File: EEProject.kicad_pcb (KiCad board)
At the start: 2 copper layers, 155.4 x 20 mm, 0 parts

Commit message: Seperated Schematics
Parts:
- added P1: USB_C_Plug_USB2.0, Connector_USB:USB_C_Plug_Molex_105444, F.Cu at (104.8, 93.5)
- added U1: ATmega328-A, Package_QFP:TQFP-32_7x7mm_P0.8mm, F.Cu at (218.8, 98.3)
- added U2: 74AHC595, Package_SO:TSSOP-16_4.4x5mm_P0.65mm, F.Cu at (145.9, 94.1)
- added U3: 74AHC595, Package_SO:TSSOP-16_4.4x5mm_P0.65mm, F.Cu at (154.5, 94.0)
- added U4: 74AHC595, Package_SO:TSSOP-16_4.4x5mm_P0.65mm, F.Cu at (163.6, 94.1)
- added U5: 74AHC595, Package_SO:TSSOP-16_4.4x5mm_P0.65mm, F.Cu at (173.0, 94.0)
- added U6: CP2102N-Axx-xQFN28, Package_DFN_QFN:QFN-28-1EP_5x5mm_P0.5mm_EP3.35x3.35mm, F.Cu at (119.5, 93.5)

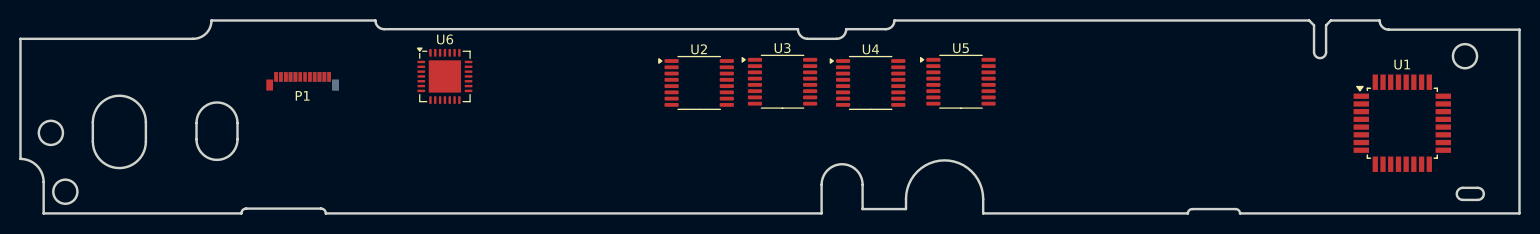
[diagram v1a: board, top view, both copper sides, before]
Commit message: Keyboard Data Changes and added footprints
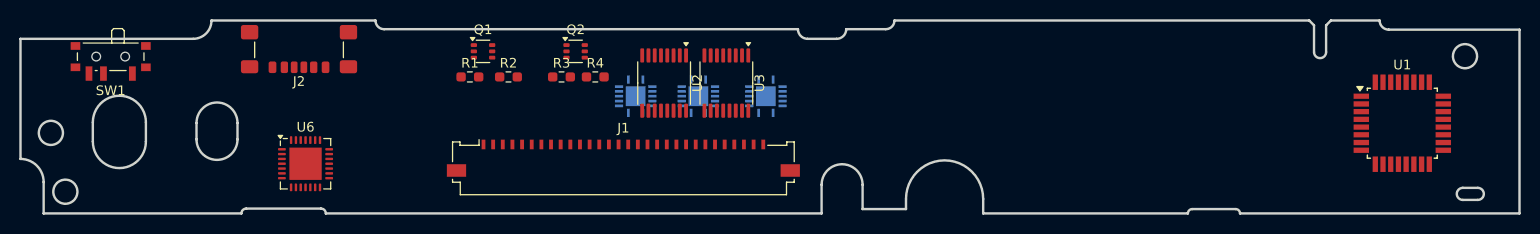
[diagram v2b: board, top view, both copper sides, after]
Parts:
- removed P1: USB_C_Plug_USB2.0, Connector_USB:USB_C_Plug_Molex_105444
- added J1: Flex_Cable_Connector_1.0_1x30, Connector_FFC-FPC:Molex_200528-0300_1x30-1MP_P1.00mm_Horizontal, F.Cu at (138.0, 101.4)
- added J2: USB_C_Receptacle_USB2.0_14P, Connector_USB:USB_C_Receptacle_GCT_USB4135-GF-A_6P_TopMnt_Horizontal, F.Cu at (104.4, 89.5)
- added Q1: PUMX1, Package_TO_SOT_SMD:SOT-363_SC-70-6, F.Cu at (123.5, 90.8)
- added Q2: PUMX1, Package_TO_SOT_SMD:SOT-363_SC-70-6, F.Cu at (133.1, 90.8)
- added R1: R, Resistor_SMD:R_0603_1608Metric_Pad0.98x0.95mm_HandSolder, F.Cu at (122.1, 93.5)
- added R2: R, Resistor_SMD:R_0603_1608Metric_Pad0.98x0.95mm_HandSolder, F.Cu at (126.1, 93.5)
- added R3: R, Resistor_SMD:R_0603_1608Metric_Pad0.98x0.95mm_HandSolder, F.Cu at (131.6, 93.5)
- added R4: R, Resistor_SMD:R_0603_1608Metric_Pad0.98x0.95mm_HandSolder, F.Cu at (135.1, 93.5)
- added SW1: SW_SPDT, Button_Switch_SMD:SW_SPDT_PCM12, F.Cu at (84.8, 91.7)
- added U7: VC07A, Package_DFN_QFN:Texas_S-PVQFN-N14, B.Cu at (145.8, 95.5)
- U2, U3: value 74AHC595 -> 74HC595
- U4, U5: value 74AHC595 -> VC07A; footprint Package_SO:TSSOP-16_4.4x5mm_P0.65mm -> Package_DFN_QFN:Texas_S-PVQFN-N14; moved to B.Cu
- moved U4 24.4 mm to (139.3, 95.5), turned to 180 degrees
- moved U5 20.3 mm to (152.8, 95.5), turned to 180 degrees
- moved U6 17.1 mm to (105.0, 102.5)
- moved U3 5.83 mm to (148.7, 94.1), turned to -90 degrees
- moved U2 3.64 mm to (142.2, 94.1), turned to -90 degrees
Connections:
- U2 pad 1: unconnected-(U2-QB-Pad1) -> Net-(U2-QB)
- U2 pad 15: unconnected-(U2-QA-Pad15) -> Net-(U2-QA)
- U2 pad 2: unconnected-(U2-QC-Pad2) -> Net-(U2-QC)
- U2 pad 3: unconnected-(U2-QD-Pad3) -> Net-(U2-QD)
- U2 pad 4: unconnected-(U2-QE-Pad4) -> Net-(U2-QE)
- U2 pad 5: unconnected-(U2-QF-Pad5) -> Net-(U2-QF)
- U2 pad 6: unconnected-(U2-QG-Pad6) -> Net-(U2-QG)
- U2 pad 7: unconnected-(U2-QH-Pad7) -> Net-(U2-QH)
- U3 pad 1: unconnected-(U3-QB-Pad1) -> Net-(U3-QB)
- U3 pad 15: unconnected-(U3-QA-Pad15) -> Net-(U3-QA)
- U3 pad 2: unconnected-(U3-QC-Pad2) -> Net-(U3-QC)
- U3 pad 3: unconnected-(U3-QD-Pad3) -> Net-(U3-QD)
- U3 pad 4: unconnected-(U3-QE-Pad4) -> Net-(U3-QE)
- U3 pad 5: unconnected-(U3-QF-Pad5) -> Net-(U3-QF)
- U3 pad 6: unconnected-(U3-QG-Pad6) -> Net-(U3-QG)
- U3 pad 7: unconnected-(U3-QH-Pad7) -> Net-(U3-QH)
- U4 pad 1: unconnected-(U4-QB-Pad1) -> Net-(U2-QA)
- U4 pad 10: unconnected-(U4-~{SRCLR}-Pad10) -> Net-(J1-Pin_12)
- U4 pad 11: unconnected-(U4-SRCLK-Pad11) -> Net-(U2-QE)
- U4 pad 12: unconnected-(U4-RCLK-Pad12) -> Net-(J1-Pin_11)
- U4 pad 13: unconnected-(U4-~{OE}-Pad13) -> Net-(U2-QF)
- U4 pad 15: unconnected-(U4-QA-Pad15) -> (no net)
- U4 pad 2: unconnected-(U4-QC-Pad2) -> Net-(J1-Pin_16)
- U4 pad 3: unconnected-(U4-QD-Pad3) -> Net-(U2-QB)
- U4 pad 4: unconnected-(U4-QE-Pad4) -> Net-(J1-Pin_15)
- U4 pad 5: unconnected-(U4-QF-Pad5) -> Net-(U2-QC)
- U4 pad 6: unconnected-(U4-QG-Pad6) -> Net-(J1-Pin_14)
- U4 pad 8: unconnected-(U4-GND-Pad8) -> Net-(J1-Pin_13)
- U4 pad 9: unconnected-(U4-QH'-Pad9) -> Net-(U2-QD)
- U5 pad 1: unconnected-(U5-QB-Pad1) -> Net-(U2-QG)
- U5 pad 10: unconnected-(U5-~{SRCLR}-Pad10) -> Net-(J1-Pin_6)
- U5 pad 11: unconnected-(U5-SRCLK-Pad11) -> Net-(U3-QC)
- U5 pad 12: unconnected-(U5-RCLK-Pad12) -> Net-(J1-Pin_5)
- U5 pad 13: unconnected-(U5-~{OE}-Pad13) -> Net-(U3-QD)
- U5 pad 15: unconnected-(U5-QA-Pad15) -> (no net)
- U5 pad 2: unconnected-(U5-QC-Pad2) -> Net-(J1-Pin_10)
- U5 pad 3: unconnected-(U5-QD-Pad3) -> Net-(U2-QH)
- U5 pad 4: unconnected-(U5-QE-Pad4) -> Net-(J1-Pin_9)
- U5 pad 5: unconnected-(U5-QF-Pad5) -> Net-(U3-QA)
- U5 pad 6: unconnected-(U5-QG-Pad6) -> Net-(J1-Pin_8)
- U5 pad 8: unconnected-(U5-GND-Pad8) -> Net-(J1-Pin_7)
- U5 pad 9: unconnected-(U5-QH'-Pad9) -> Net-(U3-QB)

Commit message: Atmega34u4
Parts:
- removed SW1: SW_SPDT, Button_Switch_SMD:SW_SPDT_PCM12
- removed U6: CP2102N-Axx-xQFN28, Package_DFN_QFN:QFN-28-1EP_5x5mm_P0.5mm_EP3.35x3.35mm
- U1: value ATmega328-A -> ATmega32U4-A; footprint Package_QFP:TQFP-32_7x7mm_P0.8mm -> Package_QFP:TQFP-44_10x10mm_P0.8mm
- U4, U5, U7: footprint Package_DFN_QFN:Texas_S-PVQFN-N14 -> Package_SO:TSSOP-14_4.4x5mm_P0.65mm
- moved Q1 36.7 mm to (160.1, 93.2)
- moved U1 34.8 mm to (184.0, 97.7)
- moved R1 34.0 mm to (156.0, 91.5)
- moved R2 29.9 mm to (156.0, 94.0)
- moved Q2 27.6 mm to (160.1, 96.7)
- moved R3 24.5 mm to (156.0, 96.0)
- moved R4 21.4 mm to (156.0, 98.0)
- moved U4 8.79 mm to (130.5, 95.0), turned to 90 degrees
- moved U7 6.24 mm to (139.6, 95.1), turned to 90 degrees
- moved U5 5.24 mm to (147.6, 95.1), turned to 90 degrees
- moved U2 1.20 mm to (141.0, 94.1)
- moved U3 0.84 mm to (149.5, 94.0)
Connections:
- U1 pad 14: unconnected-(U1-PB2-Pad14) -> VCC
- U1 pad 15: unconnected-(U1-PB3-Pad15) -> Net-(U1-GND-Pad15)
- U1 pad 21: Net-(U1-GND-Pad21) -> unconnected-(U1-PD3-Pad21)
- U1 pad 23: unconnected-(U1-PC0-Pad23) -> Net-(U1-GND-Pad15)
- U1 pad 24: unconnected-(U1-PC1-Pad24) -> Net-(U1-AVCC-Pad24)
- U1 pad 3: Net-(U1-GND-Pad21) -> unconnected-(U1-D--Pad3)
- U1 pad 4: VCC -> unconnected-(U1-D+-Pad4)
- U1 pad 5: Net-(U1-GND-Pad21) -> unconnected-(U1-UGND-Pad5)
- U1 pad 6: VCC -> unconnected-(U1-UCAP-Pad6)
